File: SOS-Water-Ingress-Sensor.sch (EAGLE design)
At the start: 12 parts

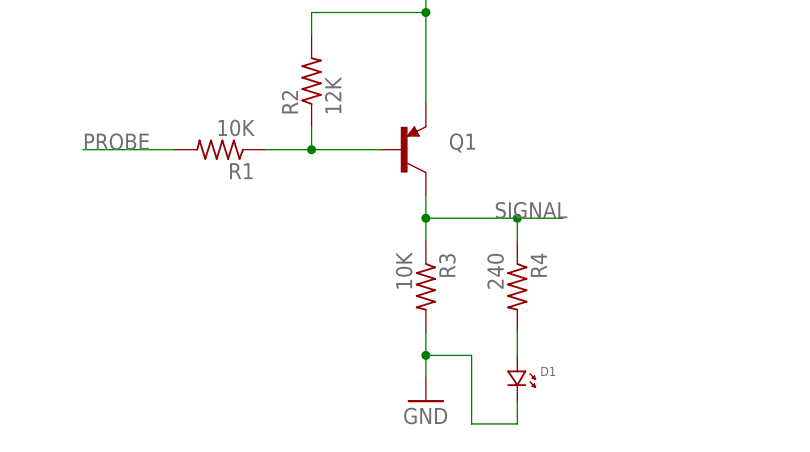
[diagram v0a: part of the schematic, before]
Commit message: Updated pull-down resistor to 2.2k.
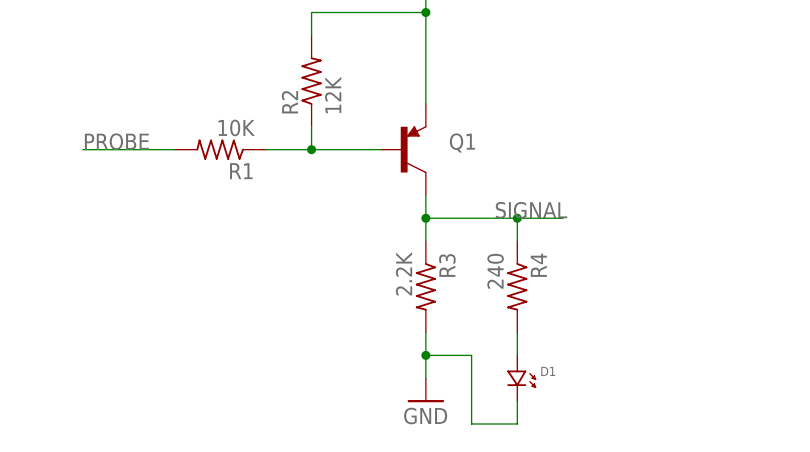
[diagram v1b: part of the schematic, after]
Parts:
- R3: value 10K -> 2.2K
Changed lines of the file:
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@@
 <?xml version="1.0" encoding="utf-8"?>
 <!DOCTYPE eagle SYSTEM "eagle.dtd">
-<eagle version="7.4.0">
+<eagle version="7.6.0">
 <drawing>
 <settings>
@@
 <grid distance="0.1" unitdist="inch" unit="inch" style="lines" multiple="1" display="no" altdistance="0.01" altunitdist="inch" altunit="inch"/>
 <layers>
-<layer number="1" name="Top" color="4" fill="1" visible="yes" active="no"/>
-<layer number="2" name="Route2" color="1" fill="3" visible="yes" active="no"/>
-<layer number="3" name="Route3" color="4" fill="3" visible="yes" active="no"/>
-<layer number="14" name="Route14" color="1" fill="6" visible="yes" active="no"/>
-<layer number="15" name="Route15" color="4" fill="6" visible="yes" active="no"/>
-<layer number="16" name="Bottom" color="1" fill="1" visible="yes" active="no"/>
-<layer number="17" name="Pads" color="2" fill="1" visible="yes" active="no"/>
-<layer number="18" name="Vias" color="2" fill="1" visible="yes" active="no"/>
-<layer number="19" name="Unrouted" color="6" fill="1" visible="yes" active="no"/>
-<layer number="20" name="Dimension" color="15" fill="1" visible="yes" active="no"/>
-<layer number="21" name="tPlace" color="7" fill="1" visible="yes" active="no"/>
-<layer number="22" name="bPlace" color="7" fill="1" visible="yes" active="no"/>
-<layer number="23" name="tOrigins" color="15" fill="1" visible="yes" active="no"/>
-<layer number="24" name="bOrigins" color="15" fill="1" visible="yes" active="no"/>
-<layer number="25" name="tNames" color="7" fill="1" visible="yes" active="no"/>
-<layer number="26" name="bNames" color="7" fill="1" visible="yes" active="no"/>
-<layer number="27" name="tValues" color="7" fill="1" visible="yes" active="no"/>
-<layer number="28" name="bValues" color="7" fill="1" visible="yes" active="no"/>
+<layer number="1" name="Top" color="4" fill="1" visible="no" active="no"/>
+<layer number="2" name="Route2" color="1" fill="3" visible="no" active="no"/>
+<layer number="3" name="Route3" color="4" fill="3" visible="no" active="no"/>
+<layer number="14" name="Route14" color="1" fill="6" visible="no" active="no"/>
+<layer number="15" name="Route15" color="4" fill="6" visible="no" active="no"/>
+<layer number="16" name="Bottom" color="1" fill="1" visible="no" active="no"/>
+<layer number="17" name="Pads" color="2" fill="1" visible="no" active="no"/>
+<layer number="18" name="Vias" color="2" fill="1" visible="no" active="no"/>
+<layer number="19" name="Unrouted" color="6" fill="1" visible="no" active="no"/>
+<layer number="20" name="Dimension" color="15" fill="1" visible="no" active="no"/>
+<layer number="21" name="tPlace" color="7" fill="1" visible="no" active="no"/>
+<layer number="22" name="bPlace" color="7" fill="1" visible="no" active="no"/>
+<layer number="23" name="tOrigins" color="15" fill="1" visible="no" active="no"/>
+<layer number="24" name="bOrigins" color="15" fill="1" visible="no" active="no"/>
+<layer number="25" name="tNames" color="7" fill="1" visible="no" active="no"/>
+<layer number="26" name="bNames" color="7" fill="1" visible="no" active="no"/>
+<layer number="27" name="tValues" color="7" fill="1" visible="no" active="no"/>
+<layer number="28" name="bValues" color="7" fill="1" visible="no" active="no"/>
 <layer number="29" name="tStop" color="7" fill="3" visible="no" active="no"/>
 <layer number="30" name="bStop" color="7" fill="6" visible="no" active="no"/>
@@
 <layer number="35" name="tGlue" color="7" fill="4" visible="no" active="no"/>
 <layer number="36" name="bGlue" color="7" fill="5" visible="no" active="no"/>
-<layer number="37" name="tTest" color="7" fill="1" visible="yes" active="no"/>
-<layer number="38" name="bTest" color="7" fill="1" visible="yes" active="no"/>
+<layer number="37" name="tTest" color="7" fill="1" visible="no" active="no"/>
+<layer number="38" name="bTest" color="7" fill="1" visible="no" active="no"/>
 <layer number="39" name="tKeepout" color="4" fill="11" visible="no" active="no"/>
 <layer number="40" name="bKeepout" color="1" fill="11" visible="no" active="no"/>
@@
 <layer number="44" name="Drills" color="7" fill="1" visible="no" active="no"/>
 <layer number="45" name="Holes" color="7" fill="1" visible="no" active="no"/>
-<layer number="46" name="Milling" color="3" fill="1" visible="yes" active="no"/>
-<layer number="47" name="Measures" color="7" fill="1" visible="yes" active="no"/>
-<layer number="48" name="Document" color="7" fill="1" visible="yes" active="no"/>
-<layer number="49" name="Reference" color="7" fill="1" visible="yes" active="no"/>
-<layer number="50" name="dxf" color="7" fill="1" visible="yes" active="no"/>
-<layer number="51" name="tDocu" color="7" fill="1" visible="yes" active="no"/>
-<layer number="52" name="bDocu" color="7" fill="1" visible="yes" active="no"/>
-<layer number="53" name="tGND_GNDA" color="7" fill="9" visible="yes" active="no"/>
-<layer number="54" name="bGND_GNDA" color="1" fill="9" visible="yes" active="no"/>
-<layer number="56" name="wert" color="7" fill="1" visible="yes" active="no"/>
-<layer number="57" name="tCAD" color="7" fill="1" visible="yes" active="no"/>
-<layer number="59" name="tCarbon" color="7" fill="1" visible="yes" active="no"/>
-<layer number="60" name="bCarbon" color="7" fill="1" visible="yes" active="no"/>
+<layer number="46" name="Milling" color="3" fill="1" visible="no" active="no"/>
+<layer number="47" name="Measures" color="7" fill="1" visible="no" active="no"/>
+<layer number="48" name="Document" color="7" fill="1" visible="no" active="no"/>
+<layer number="49" name="Reference" color="7" fill="1" visible="no" active="no"/>
+<layer number="50" name="dxf" color="7" fill="1" visible="no" active="no"/>
+<layer number="51" name="tDocu" color="7" fill="1" visible="no" active="no"/>
+<layer number="52" name="bDocu" color="7" fill="1" visible="no" active="no"/>
+<layer number="53" name="tGND_GNDA" color="7" fill="9" visible="no" active="no"/>
+<layer number="54" name="bGND_GNDA" color="1" fill="9" visible="no" active="no"/>
+<layer number="56" name="wert" color="7" fill="1" visible="no" active="no"/>
+<layer number="57" name="tCAD" color="7" fill="1" visible="no" active="no"/>
+<layer number="59" name="tCarbon" color="7" fill="1" visible="no" active="no"/>
+<layer number="60" name="bCarbon" color="7" fill="1" visible="no" active="no"/>
 <layer number="90" name="Modules" color="5" fill="1" visible="yes" active="yes"/>
 <layer number="91" name="Nets" color="2" fill="1" visible="yes" active="yes"/>
@@
 <part name="U$1" library="BlueRobotics-JST-GH" deviceset="JSH-GH-2" device="VERT"/>
 <part name="Q1" library="SparkFun-DiscreteSemi" deviceset="TRANSISTOR_PNP" device="SMD"/>
-<part name="R3" library="resistor" deviceset="R-US_" device="R0603" value="10K"/>
+<part name="R3" library="resistor" deviceset="R-US_" device="R0603" value="2.2K"/>
 <part name="U$2" library="BlueRobotics-JST-GH" deviceset="JSH-GH-2" device="VERT"/>
 <part name="U$3" library="BlueRobotics-JST-GH" deviceset="JSH-GH-2" device="VERT"/>
